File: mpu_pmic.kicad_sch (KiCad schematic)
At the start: 60 parts, among them J501 36103505, U501 STPMIC1DPQR

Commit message: Update R & L BOM
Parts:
- R501: Digi-Key Part Number (none) -> P10.0KLCT-ND; MPN (none) -> ERJ-2RKF1002X; Manufacturer (none) -> Panasonic Electronic Components
- R502, R503: Digi-Key Part Number (none) -> P4.70KLCT-ND; MPN (none) -> ERJ-2RKF4701X; Manufacturer (none) -> Panasonic Electronic Components
- R504, R505, R506, R507, R508, R509: footprint (none) -> perfect_footprints:R_0402_1005Metric; Digi-Key Part Number (none) -> P0.0JCT-ND; MPN (none) -> ERJ-2GE0R00X; Manufacturer (none) -> Panasonic Electronic Components
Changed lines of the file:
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@@
 			)
 		)
-		(property "Footprint" ""
+		(property "Footprint" "perfect_footprints:R_0402_1005Metric"
 			(at 151.13 198.882 90)
 			(effects
@@
 			)
 		)
-		(property "Datasheet" ""
+		(property "Datasheet" "https://industrial.panasonic.com/ww/products/pt/general-purpose-chip-resistors/models/ERJ2GE0R00X"
 			(at 151.13 200.66 0)
 			(effects
@@
 			)
 		)
-		(property "Description" ""
+		(property "Description" "0 Ohms Jumper Chip Resistor 0402 (1005 Metric) Automotive AEC-Q200 Thick Film"
 			(at 151.13 200.66 0)
 			(effects
@@
 			)
 		)
-		(property "MPN" ""
+		(property "MPN" "ERJ-2GE0R00X"
 			(at 151.13 200.66 0)
 			(effects
@@
 			)
 		)
-		(property "Manufacturer" ""
+		(property "Manufacturer" "Panasonic Electronic Components"
 			(at 151.13 200.66 0)
 			(effects
@@
 			)
 		)
+		(property "Digi-Key Part Number" "P0.0JCT-ND"
+			(at 151.13 200.66 90)
+			(effects
+				(font
+					(size 1.27 1.27)
+				)
+				(hide yes)
+			)
+		)
 		(pin "2"
 		)
@@
 			)
 		)
-		(property "Datasheet" "https://www.we-online.com/components/products/datasheet/560112116014.pdf"
+		(property "Datasheet" "https://industrial.panasonic.com/cdbs/www-data/pdf/RDA0000/AOA0000C304.pdf"
 			(at 129.54 182.88 0)
 			(effects
@@
 			)
 		)
-		(property "Description" "Resistor"
+		(property "Description" "4.7 kOhms ±1% 0.1W, 1/10W Chip Resistor 0402 (1005 Metric) Automotive AEC-Q200 Thick Film"
 			(at 129.54 182.88 0)
 			(effects
@@
 			)
 		)
-		(property "MPN" ""
+		(property "MPN" "ERJ-2RKF4701X"
 			(at 129.54 182.88 0)
 			(effects
@@
 			)
 		)
-		(property "Manufacturer" ""
+		(property "Manufacturer" "Panasonic Electronic Components"
 			(at 129.54 182.88 0)
 			(effects
@@
 			)
 		)
+		(property "Digi-Key Part Number" "P4.70KLCT-ND"
+			(at 129.54 182.88 0)
+			(effects
+				(font
+					(size 1.27 1.27)
+				)
+				(hide yes)
+			)
+		)
 		(pin "2"
 		)
@@
 			)
 		)
-		(property "Footprint" ""
+		(property "Footprint" "perfect_footprints:R_0402_1005Metric"
 			(at 203.2 194.818 90)
 			(effects
@@
 			)
 		)
-		(property "Datasheet" ""
+		(property "Datasheet" "https://industrial.panasonic.com/ww/products/pt/general-purpose-chip-resistors/models/ERJ2GE0R00X"
 			(at 203.2 193.04 0)
 			(effects
@@
 			)
 		)
-		(property "Description" ""
+		(property "Description" "0 Ohms Jumper Chip Resistor 0402 (1005 Metric) Automotive AEC-Q200 Thick Film"
 			(at 203.2 193.04 0)
 			(effects
@@
 			)
 		)
-		(property "MPN" ""
+		(property "MPN" "ERJ-2GE0R00X"
 			(at 203.2 193.04 0)
 			(effects
@@
 			)
 		)
-		(property "Manufacturer" ""
+		(property "Manufacturer" "Panasonic Electronic Components"
 			(at 203.2 193.04 0)
 			(effects
@@
 			)
 		)
+		(property "Digi-Key Part Number" "P0.0JCT-ND"
+			(at 203.2 193.04 90)
+			(effects
+				(font
+					(size 1.27 1.27)
+				)
+				(hide yes)
+			)
+		)
 		(pin "2"
 		)
@@
 			)
 		)
-		(property "Datasheet" "https://www.we-online.com/components/products/datasheet/560112116014.pdf"
+		(property "Datasheet" "https://industrial.panasonic.com/cdbs/www-data/pdf/RDA0000/AOA0000C304.pdf"
 			(at 116.84 182.88 0)
 			(effects
@@
 			)
 		)
-		(property "Description" "Resistor"
+		(property "Description" "4.7 kOhms ±1% 0.1W, 1/10W Chip Resistor 0402 (1005 Metric) Automotive AEC-Q200 Thick Film"
 			(at 116.84 182.88 0)
 			(effects
@@
 			)
 		)
-		(property "MPN" ""
+		(property "MPN" "ERJ-2RKF4701X"
 			(at 116.84 182.88 0)
 			(effects
@@
 			)
 		)
-		(property "Manufacturer" ""
+		(property "Manufacturer" "Panasonic Electronic Components"
 			(at 116.84 182.88 0)
 			(effects
@@
 			)
 		)
+		(property "Digi-Key Part Number" "P4.70KLCT-ND"
+			(at 116.84 182.88 0)
+			(effects
+				(font
+					(size 1.27 1.27)
+				)
+				(hide yes)
+			)
+		)
 		(pin "2"
 		)
@@
 			)
 		)
-		(property "Datasheet" "https://www.we-online.com/components/products/datasheet/560112116014.pdf"
+		(property "Datasheet" "https://industrial.panasonic.com/cdbs/www-data/pdf/RDA0000/AOA0000C304.pdf"
 			(at 104.14 182.88 0)
 			(effects
@@
 			)
 		)
-		(property "Description" "Resistor"
+		(property "Description" "10 kOhms ±1% 0.1W, 1/10W Chip Resistor 0402 (1005 Metric) Automotive AEC-Q200 Thick Film"
 			(at 104.14 182.88 0)
 			(effects
@@
 			)
 		)
-		(property "MPN" ""
+		(property "MPN" "ERJ-2RKF1002X"
 			(at 104.14 182.88 0)
 			(effects
@@
 			)
 		)
-		(property "Manufacturer" ""
+		(property "Manufacturer" "Panasonic Electronic Components"
 			(at 104.14 182.88 0)
 			(effects
@@
 			)
 		)
+		(property "Digi-Key Part Number" "P10.0KLCT-ND"
+			(at 104.14 182.88 0)
+			(effects
+				(font
+					(size 1.27 1.27)
+				)
+				(hide yes)
+			)
+		)
 		(pin "2"
 		)
@@
 			)
 		)
-		(property "Footprint" ""
+		(property "Footprint" "perfect_footprints:R_0402_1005Metric"
 			(at 151.13 196.342 90)
 			(effects
@@
 			)
 		)
-		(property "Datasheet" ""
+		(property "Datasheet" "https://industrial.panasonic.com/ww/products/pt/general-purpose-chip-resistors/models/ERJ2GE0R00X"
 			(at 151.13 198.12 0)
 			(effects
@@
 			)
 		)
-		(property "Description" ""
+		(property "Description" "0 Ohms Jumper Chip Resistor 0402 (1005 Metric) Automotive AEC-Q200 Thick Film"
 			(at 151.13 198.12 0)
 			(effects
@@
 			)
 		)
-		(property "MPN" ""
+		(property "MPN" "ERJ-2GE0R00X"
 			(at 151.13 198.12 0)
 			(effects
@@
 			)
 		)
-		(property "Manufacturer" ""
+		(property "Manufacturer" "Panasonic Electronic Components"
 			(at 151.13 198.12 0)
 			(effects
@@
 			)
 		)
+		(property "Digi-Key Part Number" "P0.0JCT-ND"
+			(at 151.13 198.12 90)
+			(effects
+				(font
+					(size 1.27 1.27)
+				)
+				(hide yes)
+			)
+		)
 		(pin "2"
 		)
@@
 			)
 		)
-		(property "Footprint" ""
+		(property "Footprint" "perfect_footprints:R_0402_1005Metric"
 			(at 151.13 191.262 90)
 			(effects
@@
 			)
 		)
-		(property "Datasheet" ""
+		(property "Datasheet" "https://industrial.panasonic.com/ww/products/pt/general-purpose-chip-resistors/models/ERJ2GE0R00X"
 			(at 151.13 193.04 0)
 			(effects
@@
 			)
 		)
-		(property "Description" ""
+		(property "Description" "0 Ohms Jumper Chip Resistor 0402 (1005 Metric) Automotive AEC-Q200 Thick Film"
 			(at 151.13 193.04 0)
 			(effects
@@
 			)
 		)
-		(property "MPN" ""
+		(property "MPN" "ERJ-2GE0R00X"
 			(at 151.13 193.04 0)
 			(effects
@@
 			)
 		)
-		(property "Manufacturer" ""
+		(property "Manufacturer" "Panasonic Electronic Components"
 			(at 151.13 193.04 0)
 			(effects
@@
 			)
 		)
+		(property "Digi-Key Part Number" "P0.0JCT-ND"
+			(at 151.13 193.04 90)
+			(effects
+				(font
+					(size 1.27 1.27)
+				)
+				(hide yes)
+			)
+		)
 		(pin "2"
 		)
@@
 			)
 		)
-		(property "Footprint" ""
+		(property "Footprint" "perfect_footprints:R_0402_1005Metric"
 			(at 151.13 201.422 90)
 			(effects
@@
 			)
 		)
-		(property "Datasheet" ""
+		(property "Datasheet" "https://industrial.panasonic.com/ww/products/pt/general-purpose-chip-resistors/models/ERJ2GE0R00X"
 			(at 151.13 203.2 0)
 			(effects
@@
 			)
 		)
-		(property "Description" ""
+		(property "Description" "0 Ohms Jumper Chip Resistor 0402 (1005 Metric) Automotive AEC-Q200 Thick Film"
 			(at 151.13 203.2 0)
 			(effects
@@
 			)
 		)
-		(property "MPN" ""
+		(property "MPN" "ERJ-2GE0R00X"
 			(at 151.13 203.2 0)
 			(effects
@@
 			)
 		)
-		(property "Manufacturer" ""
+		(property "Manufacturer" "Panasonic Electronic Components"
 			(at 151.13 203.2 0)
 			(effects
@@
 			)
 		)
+		(property "Digi-Key Part Number" "P0.0JCT-ND"
+			(at 151.13 203.2 90)
+			(effects
+				(font
+					(size 1.27 1.27)
+				)
+				(hide yes)
+			)
+		)
 		(pin "2"
 		)
@@
 			)
 		)
-		(property "Footprint" ""
+		(property "Footprint" "perfect_footprints:R_0402_1005Metric"
 			(at 151.13 193.802 90)
 			(effects
@@
 			)
 		)
-		(property "Datasheet" ""
+		(property "Datasheet" "https://industrial.panasonic.com/ww/products/pt/general-purpose-chip-resistors/models/ERJ2GE0R00X"
 			(at 151.13 195.58 0)
 			(effects
@@
 			)
 		)
-		(property "Description" ""
+		(property "Description" "0 Ohms Jumper Chip Resistor 0402 (1005 Metric) Automotive AEC-Q200 Thick Film"
 			(at 151.13 195.58 0)
 			(effects
@@
 			)
 		)
-		(property "MPN" ""
+		(property "MPN" "ERJ-2GE0R00X"
 			(at 151.13 195.58 0)
 			(effects
@@
 			)
 		)
-		(property "Manufacturer" ""
+		(property "Manufacturer" "Panasonic Electronic Components"
 			(at 151.13 195.58 0)
 			(effects
@@
 			)
 		)
+		(property "Digi-Key Part Number" "P0.0JCT-ND"
+			(at 151.13 195.58 90)
+			(effects
+				(font
+					(size 1.27 1.27)
+				)
+				(hide yes)
+			)
+		)

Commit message: Fill BOM info
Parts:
- J501: footprint (none) -> RF_Shielding:Wuerth_36103205_20x20mm
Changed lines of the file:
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@@
 			)
 		)
-		(property "Footprint" ""
+		(property "Footprint" "RF_Shielding:Wuerth_36103205_20x20mm"
 			(at 182.88 91.44 0)
 			(effects

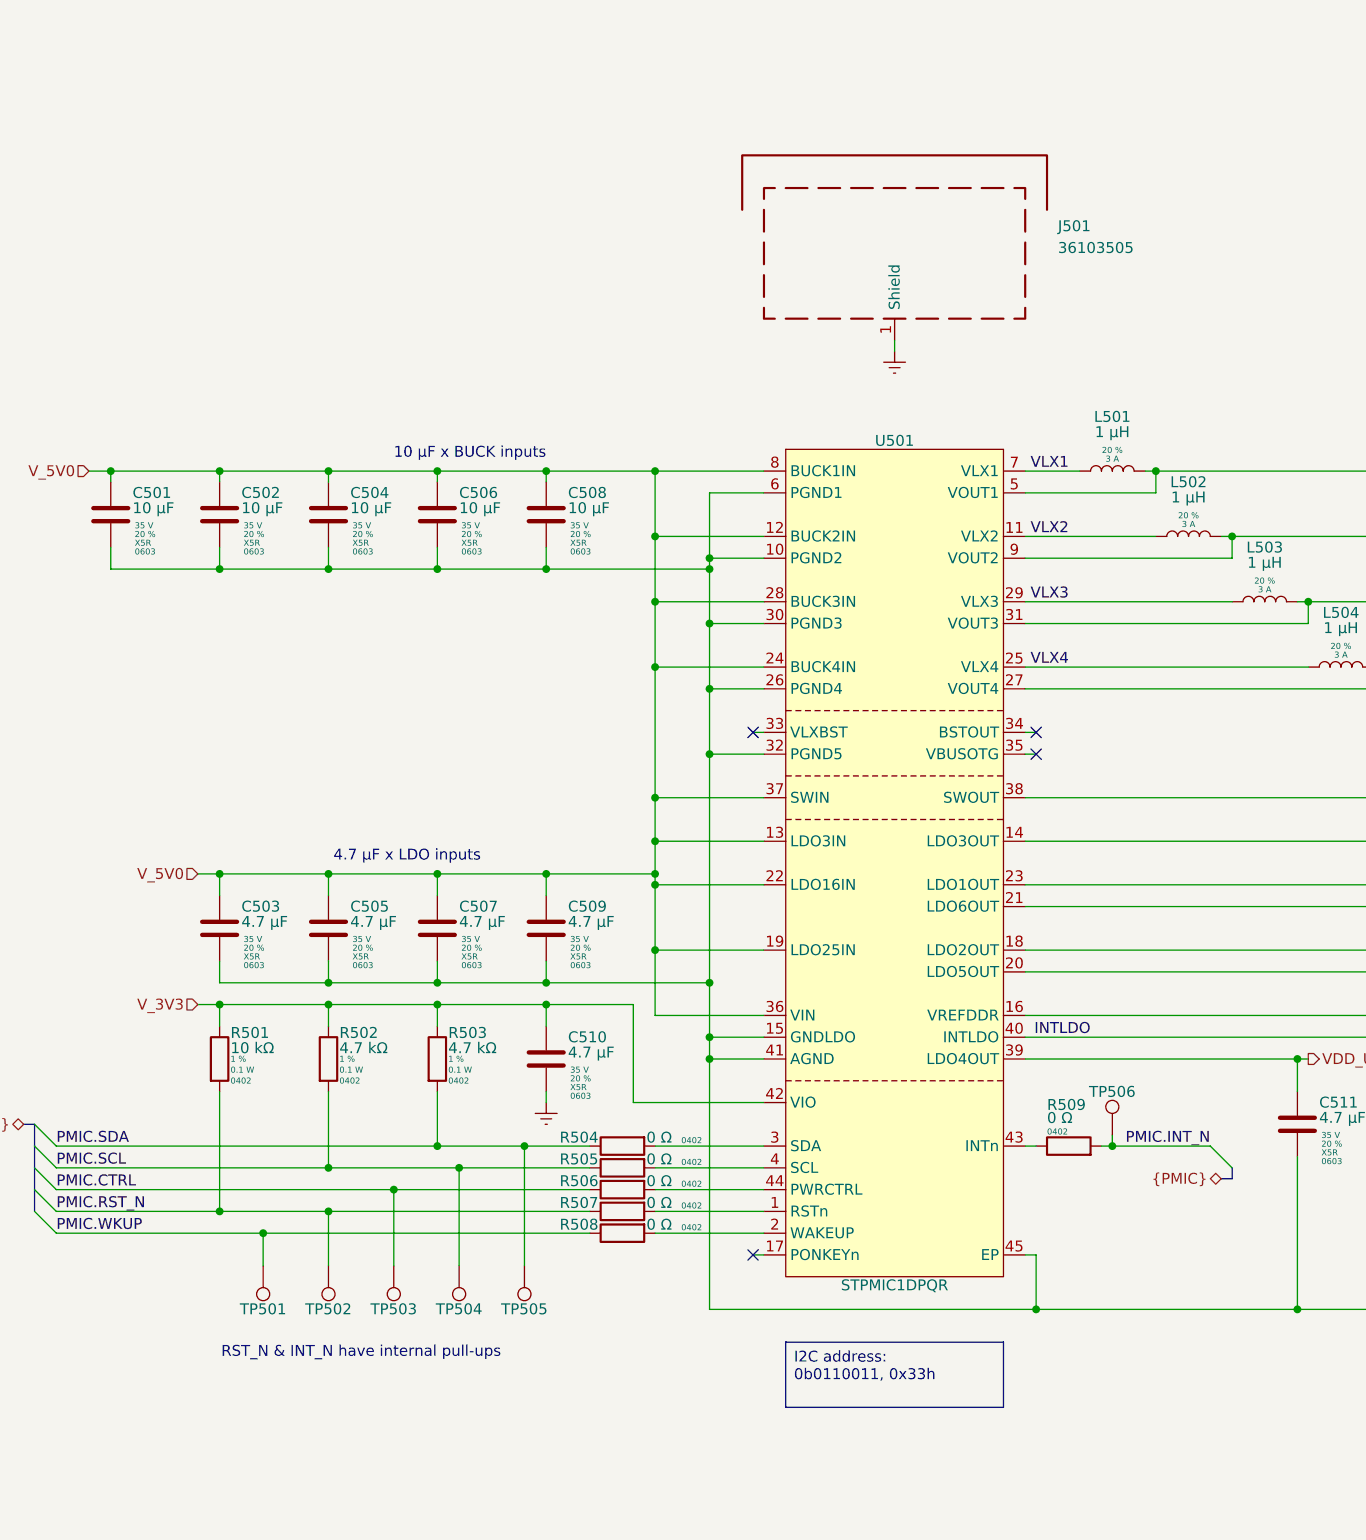
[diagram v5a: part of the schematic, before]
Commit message: Fill BOM information for the rest
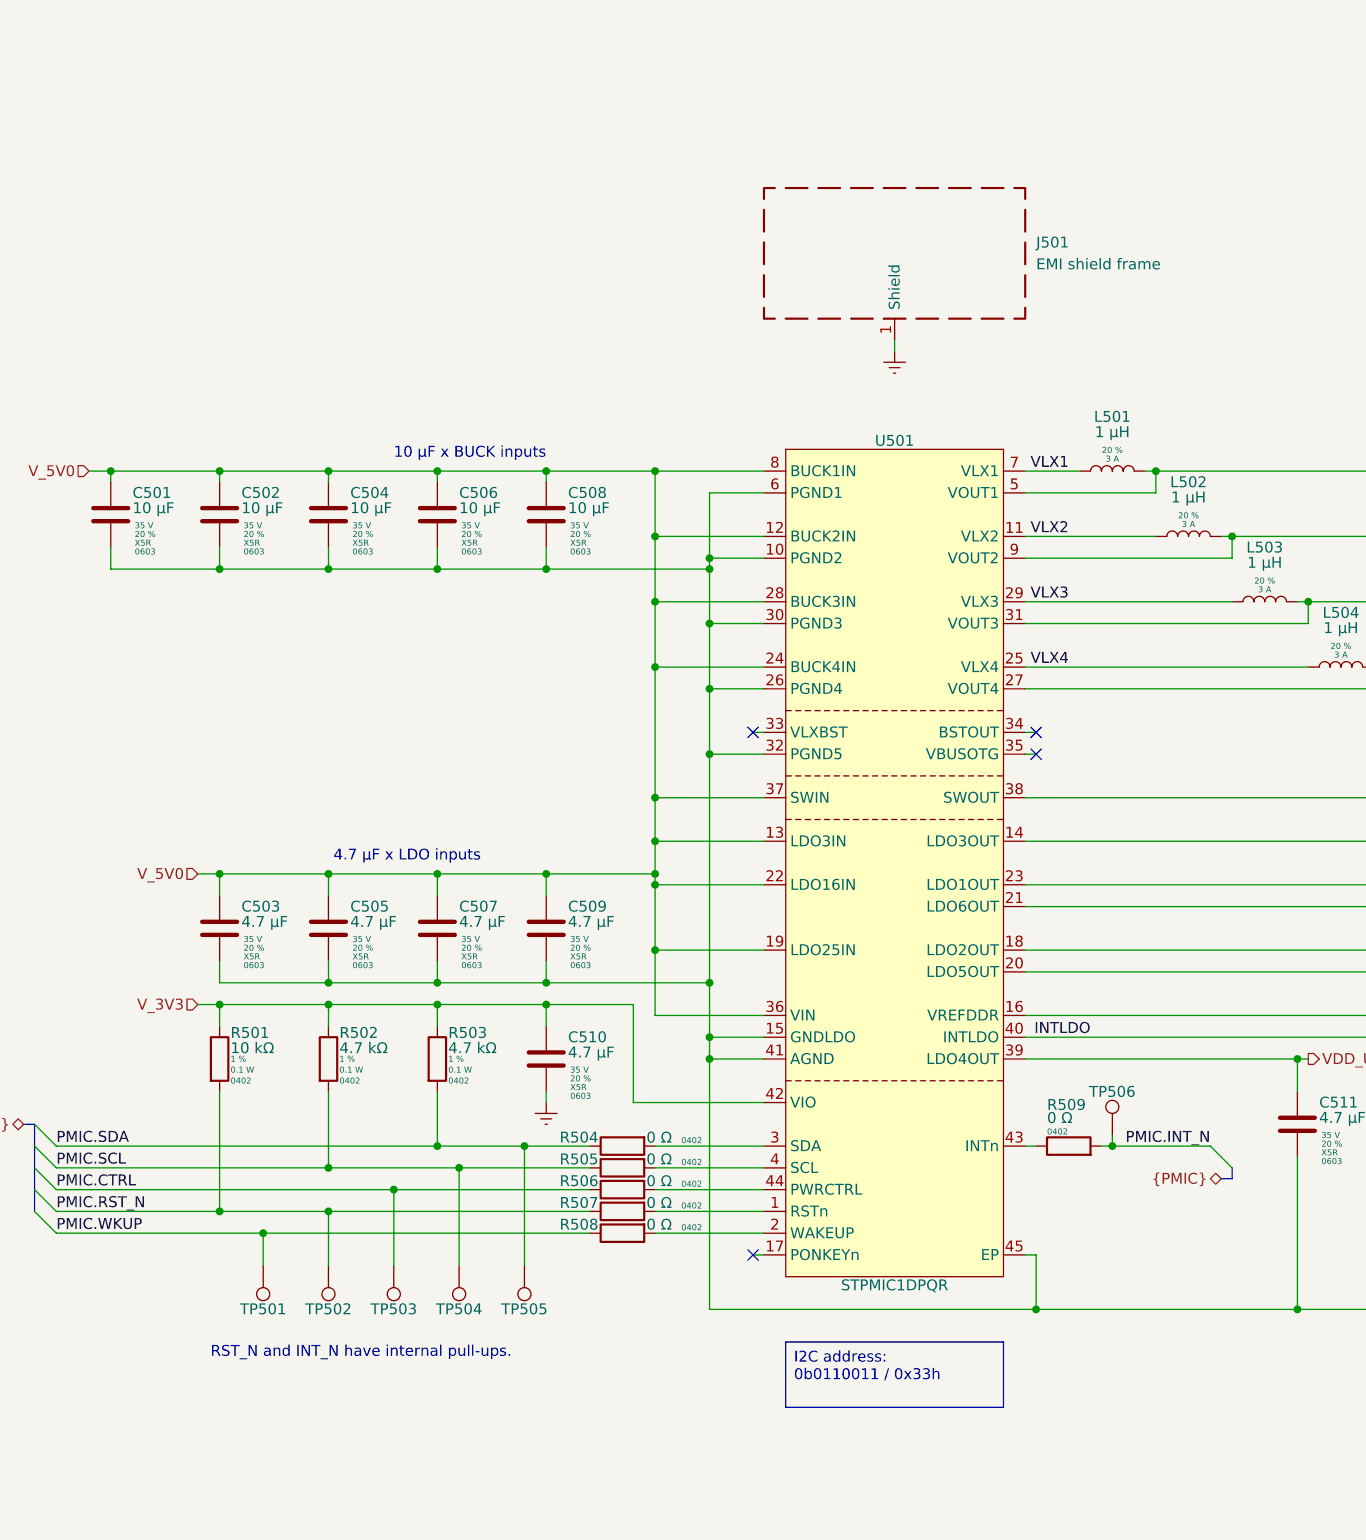
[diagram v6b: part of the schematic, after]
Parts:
- J501: value 36103505 -> EMI shield frame; footprint RF_Shielding:Wuerth_36103205_20x20mm -> RF_Shielding:Laird_Technologies_BMI-S-202-F_16.50x16.50mm; symbol Device:RFShield_TwoPieces -> Device:RFShield_OnePiece; Digi-Key Part Number (none) -> 903-1051-1-ND; MPN (none) -> BMI-S-202-F; Manufacturer (none) -> Laird Technologies EMI
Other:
- note added: "RST_N and INT_N have internal pull-ups."
- note removed: "RST_N & INT_N have internal pull-ups"
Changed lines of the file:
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@@
 		(members "PMIC.SDA" "PMIC.SCL" "PMIC.CTRL" "PMIC.RST_N" "PMIC.WKUP" "PMIC.INT_N")
 	)
-	(text "RST_N & INT_N have internal pull-ups"
+	(text "RST_N and INT_N have internal pull-ups."
 		(exclude_from_sim no)
 		(at 120.65 217.17 0)
@@
 		)
 	)
-	(text_box "I2C address:\n0b0110011, 0x33h"
+	(text_box "I2C address:\n0b0110011 / 0x33h"
 		(exclude_from_sim no)
 		(at 170.18 215.9 0)
@@
 	)
 	(symbol
-		(lib_id "Device:RFShield_TwoPieces")
+		(lib_id "Device:RFShield_OnePiece")
 		(at 182.88 88.9 0)
 		(unit 1)
@@
 		(fields_autoplaced yes)
 		(property "Reference" "J501"
-			(at 201.93 85.7249 0)
+			(at 199.39 87.6299 0)
 			(effects
 				(font
@@
 			)
 		)
-		(property "Value" "36103505"
-			(at 201.93 88.2649 0)
+		(property "Value" "EMI shield frame"
+			(at 199.39 90.1699 0)
 			(effects
 				(font
@@
 			)
 		)
-		(property "Footprint" "RF_Shielding:Wuerth_36103205_20x20mm"
+		(property "Footprint" "RF_Shielding:Laird_Technologies_BMI-S-202-F_16.50x16.50mm"
 			(at 182.88 91.44 0)
 			(effects
@@
 			)
 		)
-		(property "Datasheet" "https://www.we-online.com/components/products/datasheet/36103505.pdf"
+		(property "Datasheet" "~"
 			(at 182.88 91.44 0)
 			(effects
@@
 			)
 		)
-		(property "Description" "Two-piece EMI RF shielding cabinet"
+		(property "Description" "One-piece EMI RF shielding cabinet"
+			(at 182.88 88.9 0)
+			(effects
+				(font
+					(size 1.27 1.27)
+				)
+				(hide yes)
+			)
+		)
+		(property "Digi-Key Part Number" "903-1051-1-ND"
+			(at 182.88 88.9 0)
+			(effects
+				(font
+					(size 1.27 1.27)
+				)
+				(hide yes)
+			)
+		)
+		(property "MPN" "BMI-S-202-F"
+			(at 182.88 88.9 0)
+			(effects
+				(font
+					(size 1.27 1.27)
+				)
+				(hide yes)
+			)
+		)
+		(property "Manufacturer" "Laird Technologies EMI"
 			(at 182.88 88.9 0)
 			(effects
